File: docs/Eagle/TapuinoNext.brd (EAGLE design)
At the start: 73.6 x 44.1 mm, 8 parts

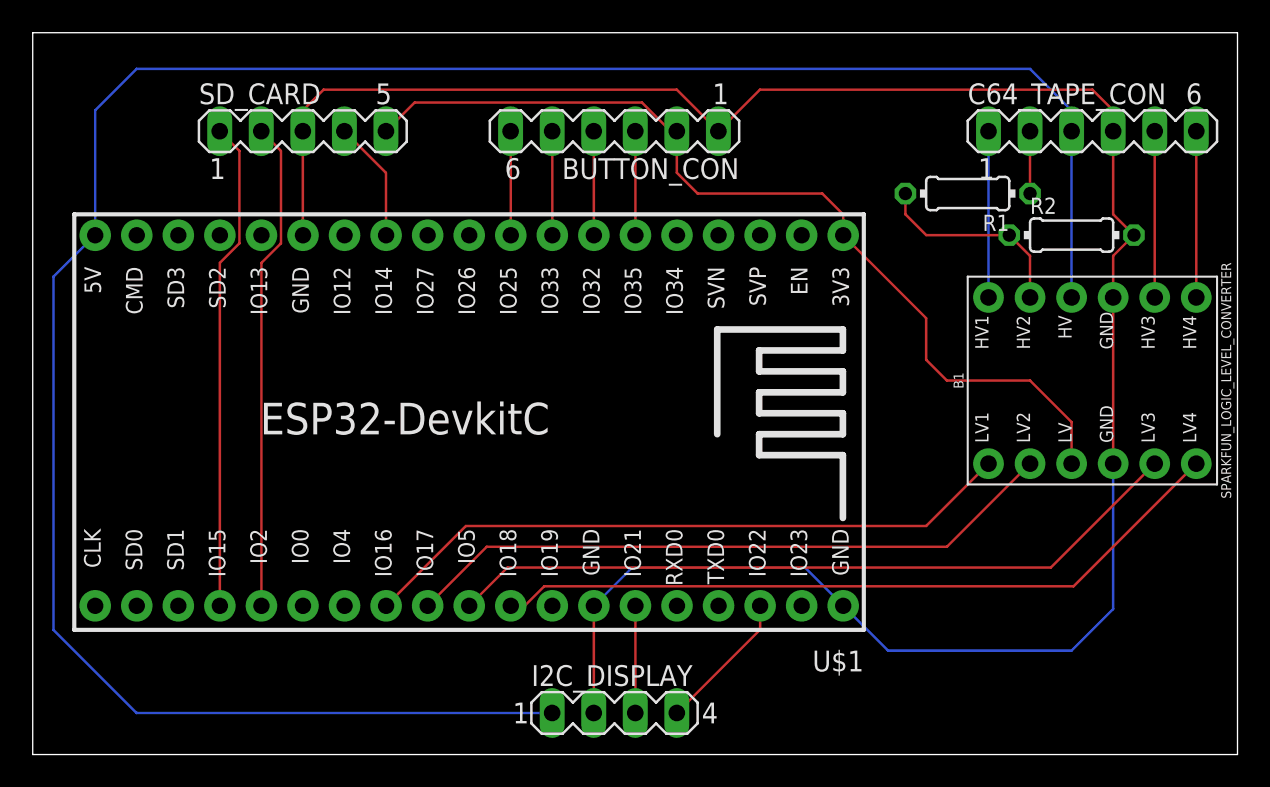
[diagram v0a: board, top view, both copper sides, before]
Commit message: add rec led and tidied up the board / schematic
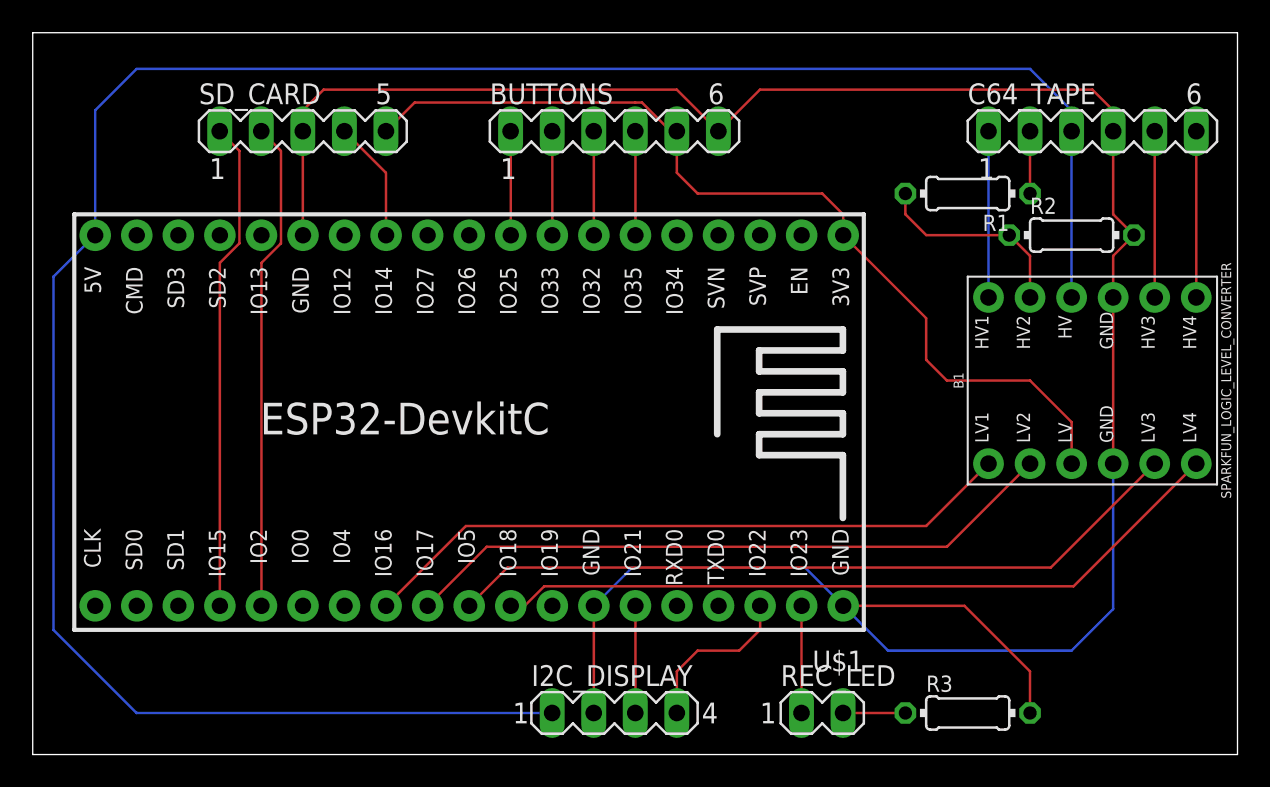
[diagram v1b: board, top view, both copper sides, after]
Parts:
- added R3: 100, rcl:0204/7
- added REC_LED: (no value), con-lstb-ext:MA02-1
- turned BUTTONS to 0 degrees
- renumbered BUTTON_CON to BUTTONS, C64_TAPE_CON to C64_TAPE
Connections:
- new net N$2: R3.1, REC_LED.2
- new net REC_LED: REC_LED.1, U$1.37
- net 3V3: now also BUTTONS.5; no longer BUTTONS.2
- net BTN_ABORT: now also BUTTONS.4; no longer BUTTONS.3
- net BTN_NEXT/ROTA: now also BUTTONS.1; no longer BUTTONS.6
- net BTN_PREV/ROTB: now also BUTTONS.3; no longer BUTTONS.4
- net BTN_SEL/ROTARY: now also BUTTONS.2; no longer BUTTONS.5
- net GND: now also BUTTONS.6, R3.2; no longer BUTTONS.1
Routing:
- net GND: track 135.0 -> 150.3 mm
- net REC_LED: track 0.00 -> 6.55 mm
- net N$2: track 0.00 -> 3.81 mm
- net SCL: track 8.66 -> 10.1 mm
